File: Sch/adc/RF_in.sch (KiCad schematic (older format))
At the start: 74 parts, among them CN1 SMA, CN2 SMA, J3 JP2, J4 JP2, J5 JP2, U1 LTC2292, U2 BGA2818, U3 TLV711, U4 BGA2818, U5 CDCLVC1102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

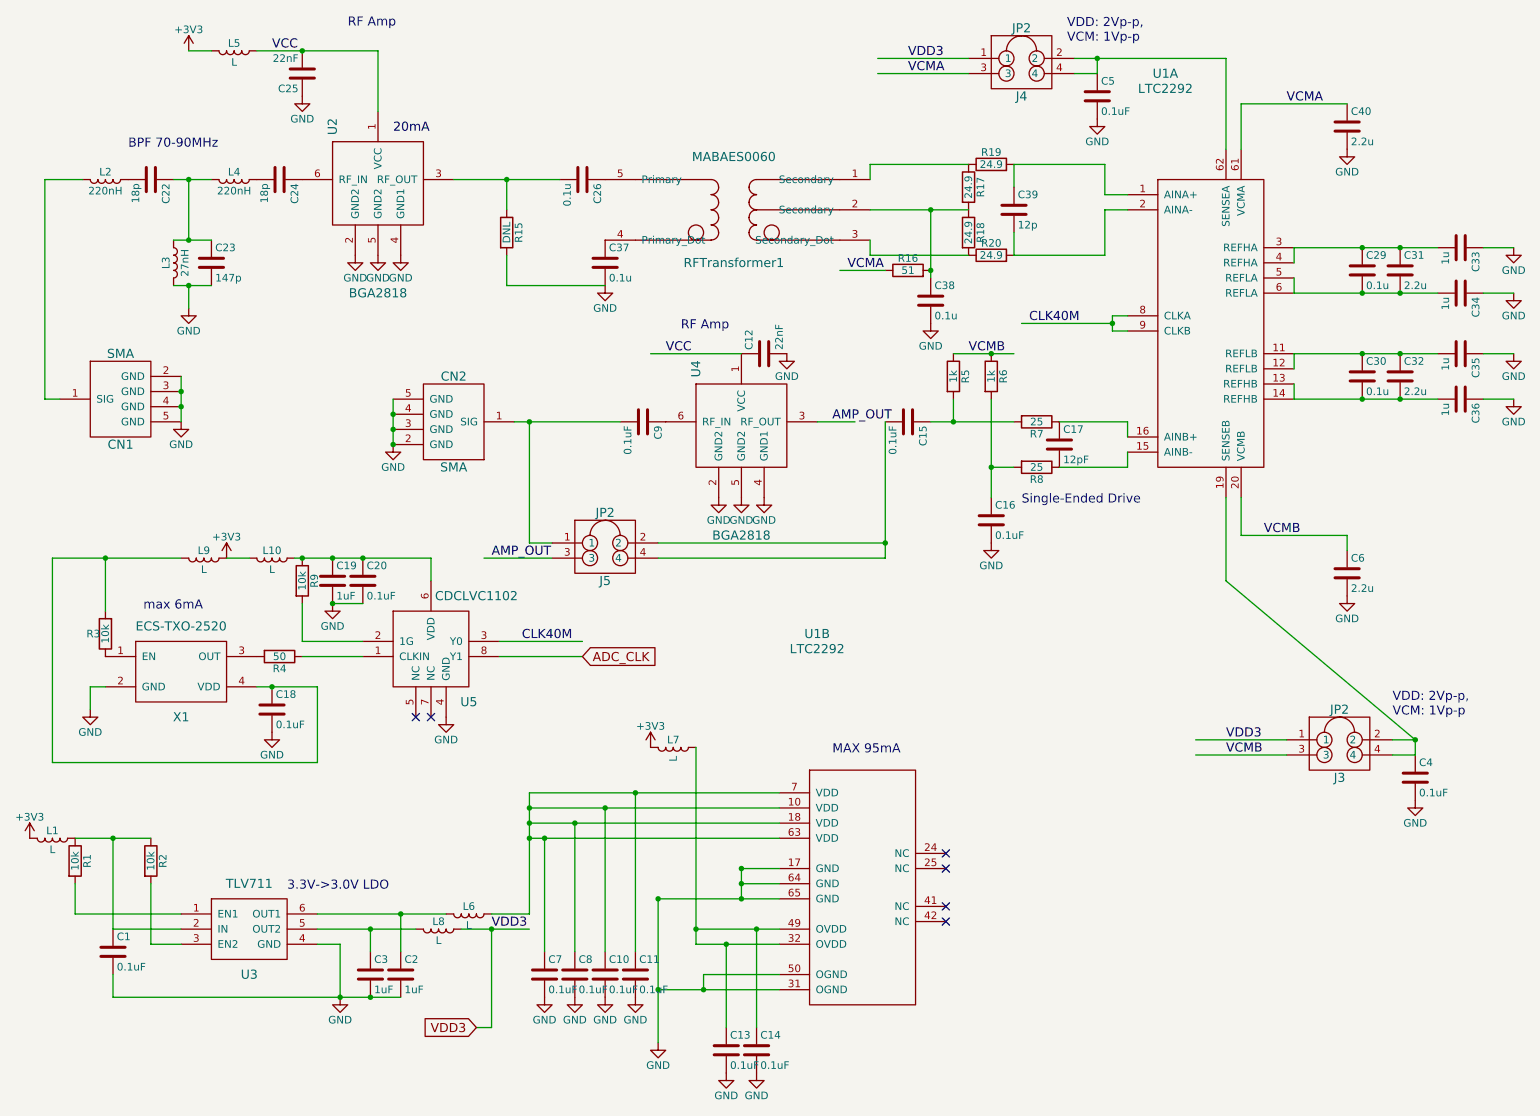
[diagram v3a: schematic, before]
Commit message: Changed LDO
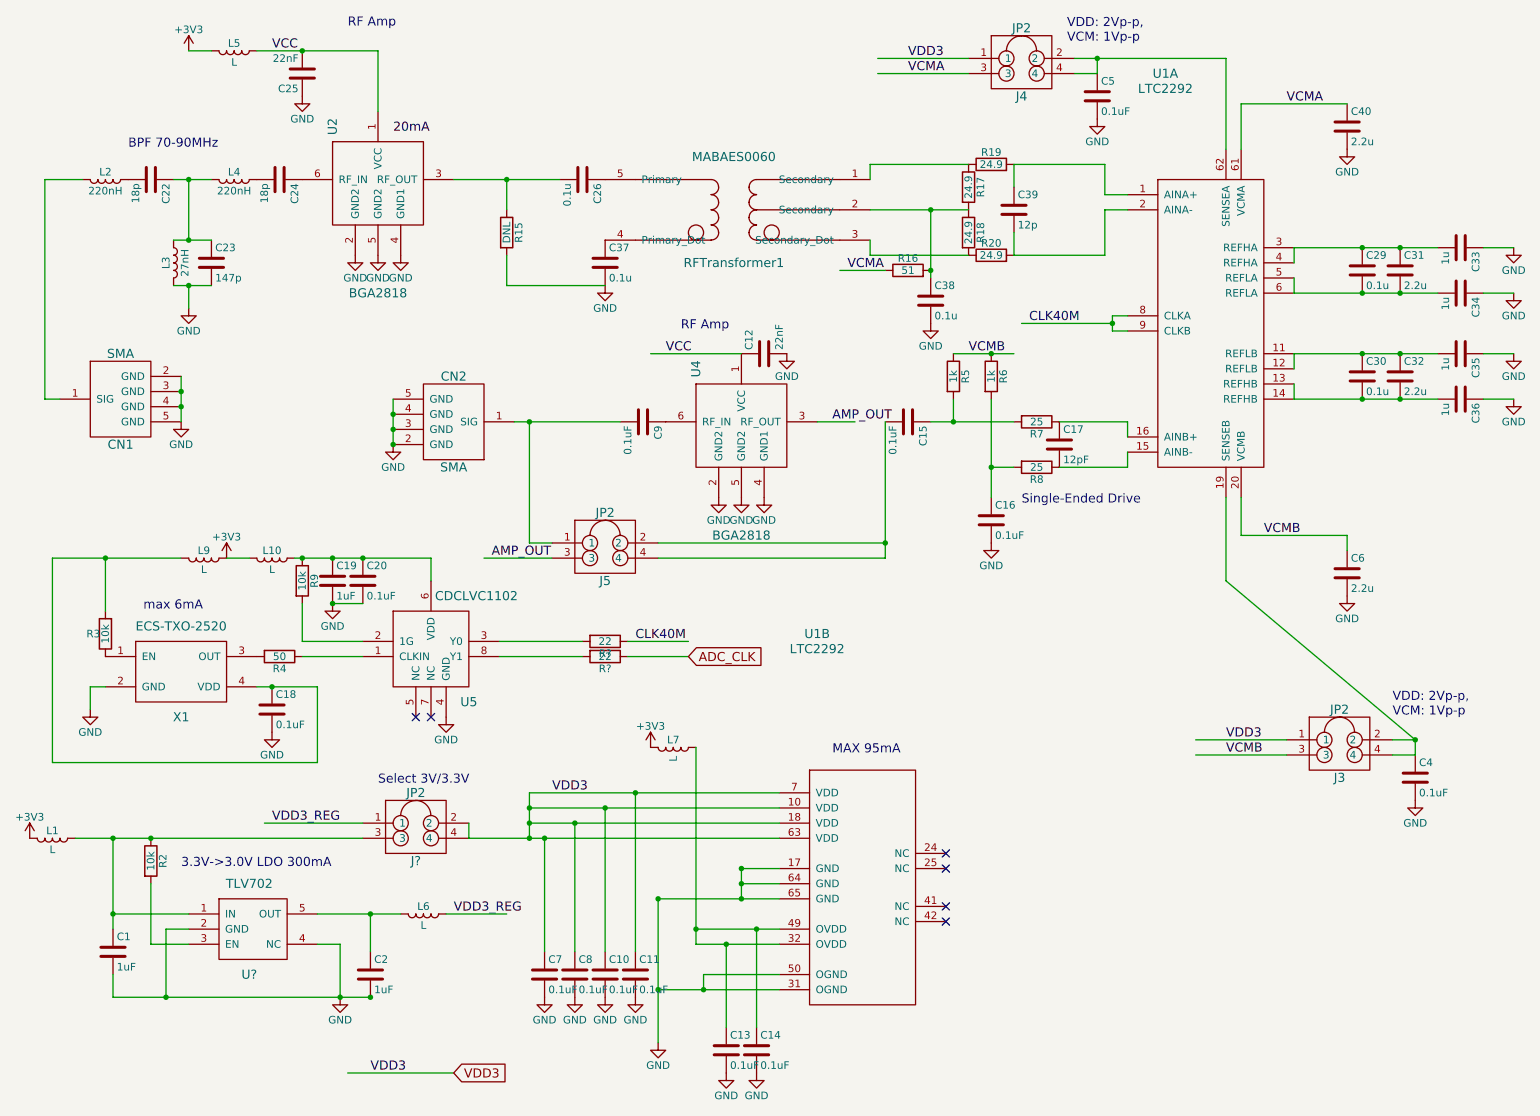
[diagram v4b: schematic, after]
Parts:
- removed C3: 1uF, symbol C
- removed L8: L, symbol L
- removed R1: 10k, symbol R
- removed U3: TLV711, symbol TLV711
- added J?: JP2, symbol JP2
- added R? (x2): 22, symbol R
- added U?: TLV702, symbol TLV702
- C1: value 0.1uF -> 1uF
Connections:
- net labels added: VDD3_REG
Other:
- note added: "3.3V->3.0V LDO 300mA"
- note added: "Select 3V/3.3V"
- note removed: "3.3V->3.0V LDO"
- moved on the sheet: C2, L6
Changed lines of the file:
@@
-$EndComp
-$Comp
-L TLV711 U3
-U 1 1 58A5E0DA
-P 2100 6550
-F 0 "U3" H 2100 6250 60  0000 C CNN
-F 1 "TLV711" H 2100 6850 60  0000 C CNN
-F 2 "" H 2100 6850 60  0001 C CNN
-F 3 "" H 2100 6850 60  0001 C CNN
-	1    2100 6550
-	1    0    0    -1
 $EndComp
 $Comp
@@
 $EndComp
 $Comp
-L R R1
-U 1 1 58A5F224
-P 950 6100
-F 0 "R1" V 1030 6100 50  0000 C CNN
-F 1 "10k" V 950 6100 50  0000 C CNN
-F 2 "" V 880 6100 50  0000 C CNN
-F 3 "" H 950 6100 50  0000 C CNN
-	1    950  6100
-	1    0    0    -1
-$EndComp
-$Comp
 L R R2
 U 1 1 58A60AAF
@@
 L C C2
 U 1 1 58A6114E
-P 3100 6850
-F 0 "C2" H 3125 6950 50  0000 L CNN
-F 1 "1uF" H 3125 6750 50  0000 L CNN
-F 2 "" H 3138 6700 50  0000 C CNN
-F 3 "" H 3100 6850 50  0000 C CNN
-	1    3100 6850
+P 2900 6850
+F 0 "C2" H 2925 6950 50  0000 L CNN
+F 1 "1uF" H 2925 6750 50  0000 L CNN
+F 2 "" H 2938 6700 50  0000 C CNN
+F 3 "" H 2900 6850 50  0000 C CNN
+	1    2900 6850
 	1    0    0    -1
 $EndComp
@@
 P 1200 6700
 F 0 "C1" H 1225 6800 50  0000 L CNN
-F 1 "0.1uF" H 1225 6600 50  0000 L CNN
+F 1 "1uF" H 1225 6600 50  0000 L CNN
 F 2 "" H 1238 6550 50  0000 C CNN
 F 3 "" H 1200 6700 50  0000 C CNN
@@
 L L L6
 U 1 1 58A6206E
-P 3550 6450
-F 0 "L6" V 3500 6450 50  0000 C CNN
-F 1 "L" V 3625 6450 50  0000 C CNN
-F 2 "" H 3550 6450 50  0000 C CNN
-F 3 "" H 3550 6450 50  0000 C CNN
-	1    3550 6450
-	0    1    1    0
-$EndComp
-Text Notes 2350 6300 0    60   ~ 0
-3.3V->3.0V LDO
+P 3250 6450
+F 0 "L6" V 3200 6450 50  0000 C CNN
+F 1 "L" V 3325 6450 50  0000 C CNN
+F 2 "" H 3250 6450 50  0000 C CNN
+F 3 "" H 3250 6450 50  0000 C CNN
+	1    3250 6450
+	0    1    1    0
+$EndComp
+Text Notes 1650 6150 0    60   ~ 0
+3.3V->3.0V LDO 300mA
 $Comp
 L L L7
@@
 	1    0    0    -1
 $EndComp
-$Comp
-L C C3
-U 1 1 58A65DDD
-P 2900 6850
-F 0 "C3" H 2925 6950 50  0000 L CNN
-F 1 "1uF" H 2925 6750 50  0000 L CNN
-F 2 "" H 2938 6700 50  0000 C CNN
-F 3 "" H 2900 6850 50  0000 C CNN
-	1    2900 6850
-	1    0    0    -1
-$EndComp
-$Comp
-L L L8
-U 1 1 58A66117
-P 3350 6550
-F 0 "L8" V 3300 6550 50  0000 C CNN
-F 1 "L" V 3425 6550 50  0000 C CNN
-F 2 "" H 3350 6550 50  0000 C CNN
-F 3 "" H 3350 6550 50  0000 C CNN
-	1    3350 6550
-	0    1    1    0
-$EndComp
-Text Label 3700 6550 0    60   ~ 0
-VDD3
+Text Label 3450 6450 0    60   ~ 0
+VDD3_REG
 $Comp
 L R R4
@@
 Text Label 8550 5400 0    60   ~ 0
 VCMB
-Text GLabel 4300 4750 2    60   Input ~ 0
+Text GLabel 5000 4750 2    60   Input ~ 0
 ADC_CLK
 $Comp
@@
 	1850 750  1700 750
 Wire Wire Line
-	950  6450 1650 6450
-Wire Wire Line
-	2550 6650 2700 6650
-Wire Wire Line
-	2700 6650 2700 7000
-Wire Wire Line
-	950  6250 950  6450
-Wire Wire Line
-	950  5950 1450 5950
+	950  5950 2850 5950
 Wire Wire Line
 	1200 5950 1200 6550
 Wire Wire Line
-	1200 6550 1650 6550
-Wire Wire Line
-	1450 6650 1650 6650
-Wire Wire Line
-	1200 7000 3100 7000
-Wire Wire Line
-	2550 6450 3400 6450
-Wire Wire Line
-	3100 6450 3100 6700
-Connection ~ 3100 6450
+	1450 6650 1700 6650
+Wire Wire Line
+	2550 6450 3100 6450
+Wire Wire Line
+	2900 6450 2900 6700
 Connection ~ 2700 7000
 Wire Wire Line
 	1200 6850 1200 7000
 Wire Wire Line
-	3950 5650 3950 6450
-Wire Wire Line
-	3950 6450 3700 6450
+	3950 5650 3950 5950
 Wire Wire Line
 	3950 5650 5600 5650
@@
 Connection ~ 3950 5850
 Wire Wire Line
-	3950 5950 5600 5950
+	3550 5950 5600 5950
 Connection ~ 3950 5950
 Wire Wire Line
@@
 	1450 6250 1450 6650
 Wire Wire Line
-	2550 6550 3200 6550
-Wire Wire Line
-	2900 6550 2900 6700
-Connection ~ 2900 6550
-Wire Wire Line
-	3500 6550 3950 6550
-Wire Wire Line
 	2150 4950 2550 4950
 Wire Wire Line
@@
 	7800 2550 7200 2550
 Connection ~ 7800 2550
-Connection ~ 2900 7000
 Wire Wire Line
 	6850 800  6250 800
@@
 	7900 3500 7900 3400
 Wire Wire Line
-	7150 3200 6600 3200
+	6600 3200 7150 3200
 Connection ~ 6750 3200
 Wire Wire Line
@@
 Wire Wire Line
 	3750 4650 4300 4650
-Text Label 3900 4650 0    60   ~ 0
+Text Label 4650 4650 0    60   ~ 0
 CLK40M
 Wire Wire Line
@@
 $EndComp
 Connection ~ 3050 3350
-Text GLabel 3600 7200 0    60   Input ~ 0
+Text GLabel 3450 7500 2    60   Input ~ 0
 VDD3
-Wire Wire Line
-	3700 6550 3700 7200
-Wire Wire Line
-	3700 7200 3600 7200
-Connection ~ 3700 6550
+$Comp
+L R R?
+U 1 1 58A858B3
+P 4450 4650
+F 0 "R?" V 4530 4650 50  0000 C CNN
+F 1 "22" V 4450 4650 50  0000 C CNN
+F 2 "" V 4380 4650 50  0000 C CNN
+F 3 "" H 4450 4650 50  0000 C CNN
+	1    4450 4650
+	0    1    1    0
+$EndComp
+$Comp
+L R R?
+U 1 1 58A8597E
+P 4450 4750
+F 0 "R?" V 4530 4750 50  0000 C CNN
+F 1 "22" V 4450 4750 50  0000 C CNN
+F 2 "" V 4380 4750 50  0000 C CNN
+F 3 "" H 4450 4750 50  0000 C CNN
+	1    4450 4750
+	0    1    1    0
+$EndComp
+Wire Wire Line
+	4600 4650 5000 4650
+Wire Wire Line
+	4600 4750 5000 4750
+$Comp
+L TLV702 U?
+U 1 1 58A87D13
+P 2100 6550
+F 0 "U?" H 2100 6250 60  0000 C CNN
+F 1 "TLV702" H 2100 6850 60  0000 C CNN
+F 2 "" H 2100 6250 60  0001 C CNN
+F 3 "" H 2100 6250 60  0001 C CNN
+	1    2100 6550
+	1    0    0    -1
+$EndComp
+Wire Wire Line
+	2550 6650 2700 6650
+Wire Wire Line
+	2700 7000 2700 6650
+Wire Wire Line
+	1700 6450 1200 6450
+Connection ~ 1200 6450
+Wire Wire Line
+	1700 6550 1550 6550
+Wire Wire Line
+	1550 6550 1550 7000
+Connection ~ 1550 7000
+Connection ~ 2900 7000
+Connection ~ 2900 6450
+Wire Wire Line
+	1200 7000 2900 7000
+$Comp
+L JP2 J?
+U 1 1 58A8A6DA
+P 3200 5850
+F 0 "J?" H 3200 5600 60  0000 C CNN
+F 1 "JP2" H 3200 6050 60  0000 C CNN
+F 2 "" H 3150 5950 60  0001 C CNN
+F 3 "" H 3150 5950 60  0001 C CNN
+	1    3200 5850
+	1    0    0    -1
+$EndComp
+Connection ~ 1450 5950
+Wire Wire Line
+	3400 6450 3800 6450
+Text Label 2250 5850 0    60   ~ 0
+VDD3_REG
+Wire Wire Line
+	2200 5850 2850 5850
+Wire Wire Line
+	3550 5850 3550 5950
+Text Label 4100 5650 0    60   ~ 0
+VDD3
+Wire Wire Line
+	2750 7500 3450 7500
+Text Label 2900 7500 0    60   ~ 0
+VDD3
+Text Notes 2950 5600 0    60   ~ 0
+Select 3V/3.3V
 $EndSCHEMATC

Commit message: DAC in progress
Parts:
- removed L10: L, symbol L
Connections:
- wire segments 142 -> 141
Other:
- moved on the sheet: L9
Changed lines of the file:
@@
 $Descr A4 11693 8268
 encoding utf-8
-Sheet 3 3
+Sheet 3 4
 Title ""
 Date ""
@@
 Text Label 8550 5400 0    60   ~ 0
 VCMB
-Text GLabel 5000 4750 2    60   Input ~ 0
+Text GLabel 5000 4750 2    60   Output ~ 0
 ADC_CLK
 $Comp
@@
 $EndComp
 Wire Wire Line
-	2400 4100 3300 4100
+	800  4100 3300 4100
 $Comp
 L +3V3 #PWR045
 U 1 1 58A88C4E
-P 1950 4100
-F 0 "#PWR045" H 1950 3950 50  0001 C CNN
-F 1 "+3V3" H 1950 4240 50  0000 C CNN
-F 2 "" H 1950 4100 50  0000 C CNN
-F 3 "" H 1950 4100 50  0000 C CNN
-	1    1950 4100
-	1    0    0    -1
-$EndComp
-$Comp
-L L L10
-U 1 1 58A88C54
-P 2250 4100
-F 0 "L10" V 2200 4100 50  0000 C CNN
-F 1 "L" V 2325 4100 50  0000 C CNN
-F 2 "" H 2250 4100 50  0000 C CNN
-F 3 "" H 2250 4100 50  0000 C CNN
-	1    2250 4100
-	0    1    1    0
-$EndComp
-Wire Wire Line
-	2100 4100 1950 4100
+P 2000 3750
+F 0 "#PWR045" H 2000 3600 50  0001 C CNN
+F 1 "+3V3" H 2000 3890 50  0000 C CNN
+F 2 "" H 2000 3750 50  0000 C CNN
+F 3 "" H 2000 3750 50  0000 C CNN
+	1    2000 3750
+	1    0    0    -1
+$EndComp
 $Comp
 L C C19
@@
 L L L9
 U 1 1 58A8A3F4
-P 1800 4100
-F 0 "L9" V 1750 4100 50  0000 C CNN
-F 1 "L" V 1875 4100 50  0000 C CNN
-F 2 "" H 1800 4100 50  0000 C CNN
-F 3 "" H 1800 4100 50  0000 C CNN
-	1    1800 4100
+P 1850 3750
+F 0 "L9" V 1800 3750 50  0000 C CNN
+F 1 "L" V 1925 3750 50  0000 C CNN
+F 2 "" H 1850 3750 50  0000 C CNN
+F 3 "" H 1850 3750 50  0000 C CNN
+	1    1850 3750
 	0    1    1    0
 $EndComp
 Wire Wire Line
 	1150 4450 1150 4100
-Wire Wire Line
-	800  4100 1650 4100
 Wire Wire Line
 	2550 4950 2550 5450
@@
 $EndComp
 Connection ~ 3050 3350
-Text GLabel 3450 7500 2    60   Input ~ 0
+Text GLabel 3450 7500 2    60   Output ~ 0
 VDD3
 $Comp
@@
 	2550 6650 2700 6650
 Wire Wire Line
-	2700 7000 2700 6650
+	2700 6650 2700 7000
 Wire Wire Line
 	1700 6450 1200 6450
@@
 Text Notes 2950 5600 0    60   ~ 0
 Select 3V/3.3V
+Wire Wire Line
+	1700 4100 1700 3750
+Connection ~ 1700 4100
 $EndSCHEMATC

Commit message: Schematics done
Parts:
- removed L7: L, symbol L
- gave numbers to parts that had none: 4
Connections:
- net labels added: VCC33
- wire segments 141 -> 142

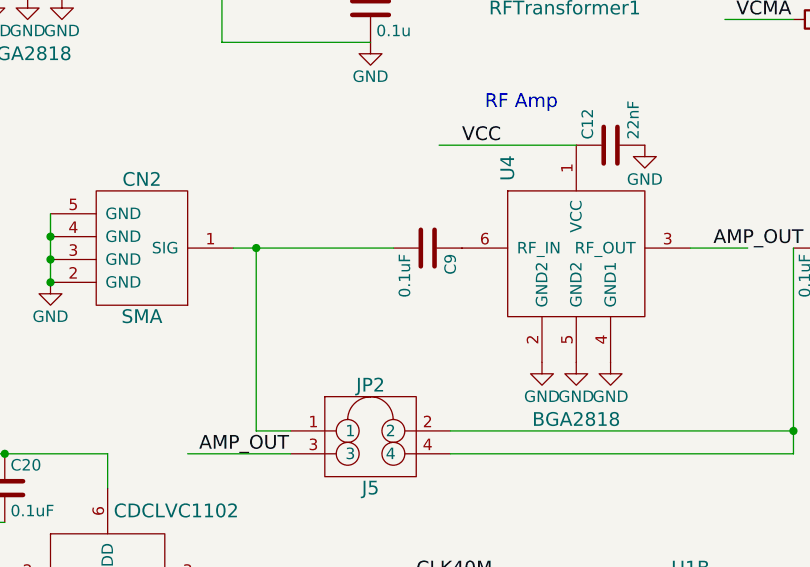
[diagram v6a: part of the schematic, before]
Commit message: Add netlist and BOM
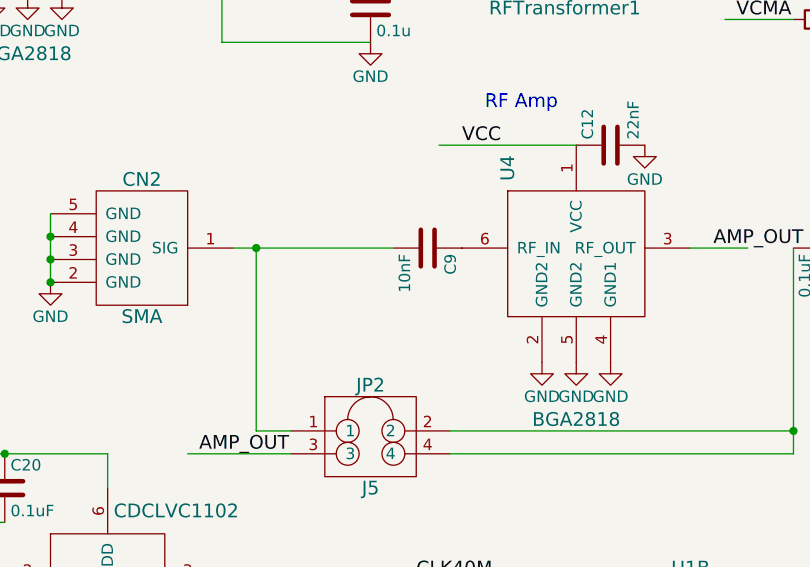
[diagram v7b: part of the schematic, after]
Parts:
- C1, C15, C16, C17, C19, C2, C20, C26, C6: footprint (none) -> Capacitors_SMD:C_0603
- C10, C11, C13, C14, C18, C4, C5, C7, C8: footprint (none) -> Capacitors_SMD:C_0402
- C9: value 0.1uF -> 10nF; footprint (none) -> Capacitors_SMD:C_0603
